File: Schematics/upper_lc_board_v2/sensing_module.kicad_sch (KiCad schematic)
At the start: 12 parts, among them J5 HALL-1, U7 ADC_ADS131M04IPWR

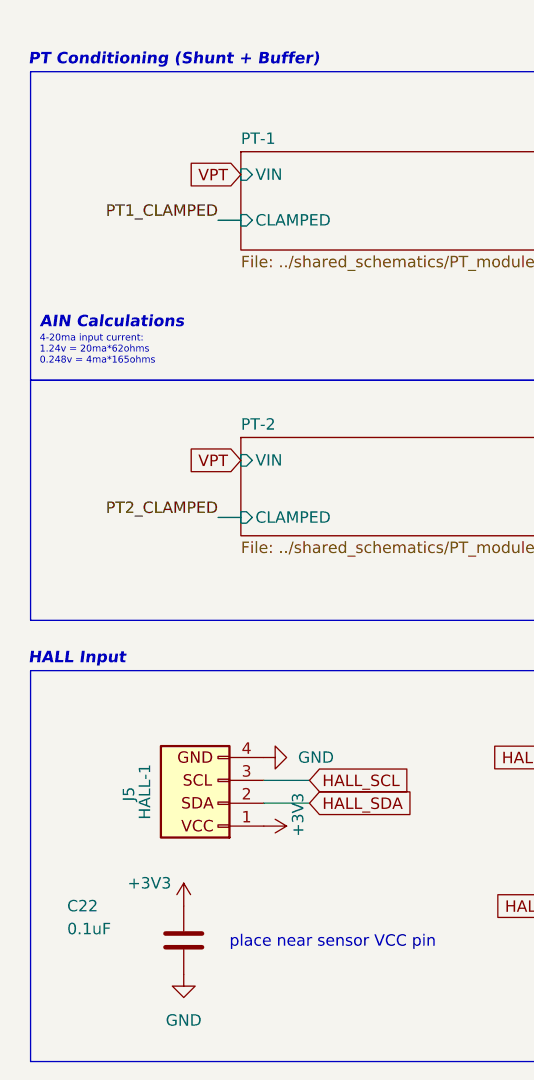
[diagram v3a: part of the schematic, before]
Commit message: updated pcb after part number and schematic fixes
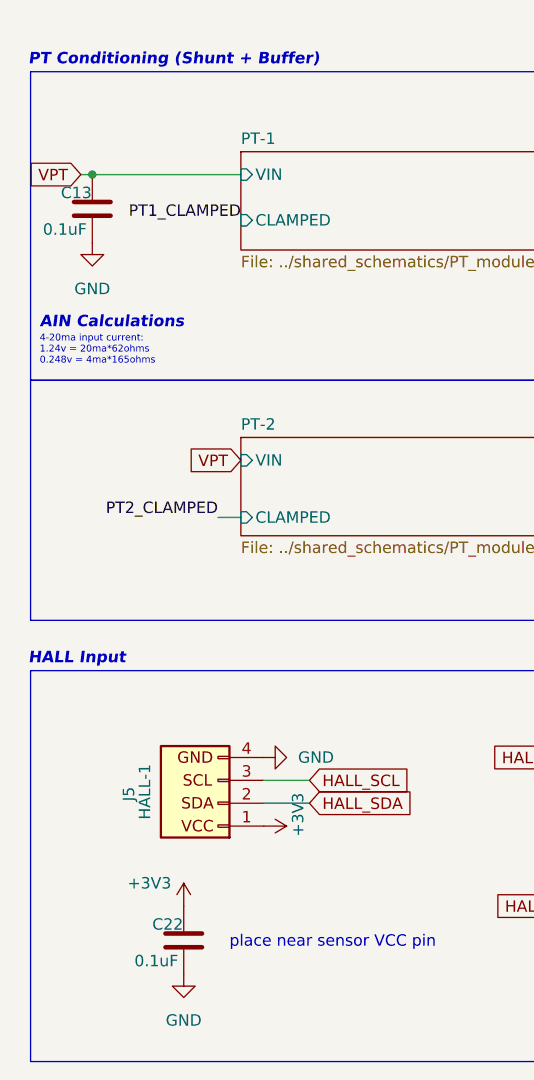
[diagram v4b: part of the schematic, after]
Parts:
- added C13: 0.1uF, Capacitor_SMD:C_0603_1608Metric, symbol Device:C
- C22: footprint Capacitor_SMD:C_0805_2012Metric -> Capacitor_SMD:C_0603_1608Metric; LCSC C49678 -> C14663
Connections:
- net GND: now also C13.2
- net VPT: now also C13.1
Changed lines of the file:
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@@
+	)
+	(junction
+		(at 59.69 55.88)
+		(diameter 0)
+		(color 0 0 0 0)
 	)
 	(junction
@@
 	(wire
 		(pts
+			(xy 58.42 55.88) (xy 59.69 55.88)
+		)
+		(stroke
+			(width 0)
+			(type default)
+		)
+	)
+	(wire
+		(pts
 			(xy 161.29 55.88) (xy 163.83 55.88)
 		)
@@
 	(wire
 		(pts
-			(xy 73.66 60.96) (xy 76.2 60.96)
-		)
-		(stroke
-			(width 0)
-			(type default)
-		)
-	)
-	(wire
-		(pts
 			(xy 170.18 67.31) (xy 172.72 67.31)
 		)
@@
 		(pts
 			(xy 172.72 77.47) (xy 172.72 74.93)
+		)
+		(stroke
+			(width 0)
+			(type default)
+		)
+	)
+	(wire
+		(pts
+			(xy 59.69 55.88) (xy 76.2 55.88)
 		)
 		(stroke
@@
 	)
 	(label "PT1_CLAMPED"
-		(at 73.66 60.96 180)
+		(at 76.2 60.96 180)
 		(fields_autoplaced yes)
 		(effects
@@
 	(global_label "VPT"
 		(shape input)
-		(at 76.2 55.88 180)
+		(at 58.42 55.88 180)
 		(fields_autoplaced yes)
 		(effects
@@
 		)
 		(property "Intersheetrefs" "${INTERSHEET_REFS}"
-			(at 69.8886 55.88 0)
+			(at 52.1086 55.88 0)
 			(effects
 				(font
@@
 	)
 	(symbol
+		(lib_id "power:GND")
+		(at 59.69 63.5 0)
+		(unit 1)
+		(exclude_from_sim no)
+		(in_bom yes)
+		(on_board yes)
+		(dnp no)
+		(fields_autoplaced yes)
+		(property "Reference" "#PWR044"
+			(at 59.69 69.85 0)
+			(effects
+				(font
+					(size 1.27 1.27)
+				)
+				(hide yes)
+			)
+		)
+		(property "Value" "GND"
+			(at 59.69 68.58 0)
+			(effects
+				(font
+					(size 1.27 1.27)
+				)
+			)
+		)
+		(property "Footprint" ""
+			(at 59.69 63.5 0)
+			(effects
+				(font
+					(size 1.27 1.27)
+				)
+				(hide yes)
+			)
+		)
+		(property "Datasheet" "https://www.ti.com/lit/ds/symlink/drv5055.pdf?HQS=dis-dk-null-digikeymode-dsf-pf-null-wwe&ts=1641231273160"
+			(at 59.69 63.5 0)
+			(effects
+				(font
+					(size 1.27 1.27)
+				)
+				(hide yes)
+			)
+		)
+		(property "Description" "Hall effect sensor."
+			(at 59.69 63.5 0)
+			(effects
+				(font
+					(size 1.27 1.27)
+				)
+				(hide yes)
+			)
+		)
+		(pin "1"
+		)
+		(instances
+			(project "upper_lc_board_v2"
+				(path "/8de962ac-ee95-4233-a205-efbcd04063bc/32a8ecec-3c56-4fc7-b1a3-95683e41c1c6"
+					(reference "#PWR044")
+					(unit 1)
+				)
+			)
+		)
+	)
+	(symbol
 		(lib_id "power:+3V3")
 		(at 78.74 128.27 270)
@@
 	)
 	(symbol
-		(lib_id "Device:C")
-		(at 69.85 140.97 0)
-		(unit 1)
-		(exclude_from_sim no)
-		(in_bom yes)
-		(on_board yes)
-		(dnp no)
-		(property "Reference" "C22"
-			(at 56.896 137.16 0)
-			(effects
-				(font
-					(size 1.27 1.27)
-				)
-				(justify left)
-			)
-		)
-		(property "Value" "0.1uF"
-			(at 56.896 139.7 0)
-			(effects
-				(font
-					(size 1.27 1.27)
-				)
-				(justify left)
-			)
-		)
-		(property "Footprint" "Capacitor_SMD:C_0805_2012Metric"
-			(at 70.8152 144.78 0)
-			(effects
-				(font
-					(size 1.27 1.27)
-				)
-				(hide yes)
-			)
-		)
-		(property "Datasheet" "~"
-			(at 69.85 140.97 0)
-			(effects
-				(font
-					(size 1.27 1.27)
-				)
-				(hide yes)
-			)
-		)
-		(property "Description" "Unpolarized capacitor"
-			(at 69.85 140.97 0)
-			(effects
-				(font
-					(size 1.27 1.27)
-				)
-				(hide yes)
-			)
-		)
-		(property "LCSC" "C49678"
-			(at 69.85 140.97 0)
-			(effects
-				(font
-					(size 1.27 1.27)
-				)
-				(hide yes)
-			)
-		)
-		(pin "2"
-		)
-		(pin "1"
-		)
-		(instances
-			(project "upper_lc_board_v2"
-				(path "/8de962ac-ee95-4233-a205-efbcd04063bc/32a8ecec-3c56-4fc7-b1a3-95683e41c1c6"
-					(reference "C22")
-					(unit 1)
-				)
-			)
-		)
-	)
-	(symbol
 		(lib_id "power:GND")
 		(at 213.36 71.12 90)
@@
 					(unit 1)
 				)
+			)
+		)
+	)
+	(symbol
+		(lib_id "Device:C")
+		(at 69.85 140.97 0)
+		(unit 1)
+		(exclude_from_sim no)
+		(in_bom yes)
+		(on_board yes)
+		(dnp no)
+		(property "Reference" "C22"
+			(at 68.072 139.192 0)
+			(effects
+				(font
+					(size 1.27 1.27)
+				)
+			)
+		)
+		(property "Value" "0.1uF"
+			(at 66.802 143.256 0)
+			(effects
+				(font
+					(size 1.27 1.27)
+				)
+			)
+		)
+		(property "Footprint" "Capacitor_SMD:C_0603_1608Metric"
+			(at 70.8152 144.78 0)
+			(effects
+				(font
+					(size 1.27 1.27)
+				)
+				(hide yes)
+			)
+		)
+		(property "Datasheet" "~"
+			(at 69.85 140.97 0)
+			(effects
+				(font
+					(size 1.27 1.27)
+				)
+				(hide yes)
+			)
+		)
+		(property "Description" "Unpolarized capacitor"
+			(at 69.85 140.97 0)
+			(effects
+				(font
+					(size 1.27 1.27)
+				)
+				(hide yes)
+			)
+		)
+		(property "LCSC" "C14663"
+			(at 69.85 140.97 90)
+			(effects
+				(font
+					(size 1.27 1.27)
+				)
+				(hide yes)
+			)
+		)
+		(pin "2"
+		)
+		(pin "1"
+		)
+		(instances
+			(project "upper_lc_board_v2"
+				(path "/8de962ac-ee95-4233-a205-efbcd04063bc/32a8ecec-3c56-4fc7-b1a3-95683e41c1c6"
+					(reference "C22")
+					(unit 1)
+				)
+			)
+		)
+	)
+	(symbol
+		(lib_id "Device:C")
+		(at 59.69 59.69 0)
+		(unit 1)
+		(exclude_from_sim no)
+		(in_bom yes)
+		(on_board yes)
+		(dnp no)
+		(property "Reference" "C13"
+			(at 57.912 57.912 0)
+			(effects
+				(font
+					(size 1.27 1.27)
+				)
+			)
+		)
+		(property "Value" "0.1uF"
+			(at 56.642 61.976 0)
+			(effects
+				(font
+					(size 1.27 1.27)
+				)
+			)
+		)
+		(property "Footprint" "Capacitor_SMD:C_0603_1608Metric"
+			(at 60.6552 63.5 0)
+			(effects
+				(font
+					(size 1.27 1.27)
+				)
+				(hide yes)
+			)
+		)
+		(property "Datasheet" "~"
+			(at 59.69 59.69 0)
+			(effects
+				(font
+					(size 1.27 1.27)
+				)
+				(hide yes)
+			)
+		)
+		(property "Description" "Unpolarized capacitor"
+			(at 59.69 59.69 0)
+			(effects
+				(font
+					(size 1.27 1.27)
+				)
+				(hide yes)
+			)
+		)
+		(property "LCSC" "C14663"
+			(at 59.69 59.69 90)
+			(effects
+				(font
+					(size 1.27 1.27)
+				)
+				(hide yes)
+			)
+		)
+		(pin "2"
+		)
+		(pin "1"
+		)
+		(instances
+			(project "upper_lc_board_v2"
+				(path "/8de962ac-ee95-4233-a205-efbcd04063bc/32a8ecec-3c56-4fc7-b1a3-95683e41c1c6"
+					(reference "C13")
+					(unit 1)
+				)
